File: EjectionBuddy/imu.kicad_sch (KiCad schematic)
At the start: 5 parts, among them U8 MPU-6050

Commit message: Side-mcu stm -> attiny, with improvements here and there
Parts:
- renumbered C18 to C17, C19 to C18, C20 to C19, C21 to C20
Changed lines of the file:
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@@
 		(on_board yes)
 		(dnp no)
-		(property "Reference" "#PWR0120"
+		(property "Reference" "#PWR0121"
 			(at 54.61 38.1 0)
 			(effects
@@
 			(project "EjectionBuddy"
 				(path "/8eb0a75f-d01a-4f77-b089-39fac6868a70/fc114c64-d761-4020-b59c-5aa26268bf21"
-					(reference "#PWR0120")
+					(reference "#PWR0121")
 					(unit 1)
 				)
@@
 		(on_board yes)
 		(dnp no)
-		(property "Reference" "C19"
+		(property "Reference" "C18"
 			(at 81.28 41.9099 0)
 			(effects
@@
 			(project "EjectionBuddy"
 				(path "/8eb0a75f-d01a-4f77-b089-39fac6868a70/fc114c64-d761-4020-b59c-5aa26268bf21"
-					(reference "C19")
+					(reference "C18")
 					(unit 1)
 				)
@@
 		(dnp no)
 		(fields_autoplaced yes)
-		(property "Reference" "#PWR0122"
+		(property "Reference" "#PWR0123"
 			(at 54.61 55.88 0)
 			(effects
@@
 			(project "EjectionBuddy"
 				(path "/8eb0a75f-d01a-4f77-b089-39fac6868a70/fc114c64-d761-4020-b59c-5aa26268bf21"
-					(reference "#PWR0122")
+					(reference "#PWR0123")
 					(unit 1)
 				)
@@
 		(dnp no)
 		(fields_autoplaced yes)
-		(property "Reference" "#PWR0125"
+		(property "Reference" "#PWR0126"
 			(at 45.72 99.06 0)
 			(effects
@@
 			(project "EjectionBuddy"
 				(path "/8eb0a75f-d01a-4f77-b089-39fac6868a70/fc114c64-d761-4020-b59c-5aa26268bf21"
-					(reference "#PWR0125")
+					(reference "#PWR0126")
 					(unit 1)
 				)
@@
 		(on_board yes)
 		(dnp no)
-		(property "Reference" "#PWR0124"
+		(property "Reference" "#PWR0125"
 			(at 92.71 68.58 0)
 			(effects
@@
 			(project "EjectionBuddy"
 				(path "/8eb0a75f-d01a-4f77-b089-39fac6868a70/fc114c64-d761-4020-b59c-5aa26268bf21"
-					(reference "#PWR0124")
+					(reference "#PWR0125")
 					(unit 1)
 				)
@@
 		(dnp no)
 		(fields_autoplaced yes)
-		(property "Reference" "#PWR0127"
+		(property "Reference" "#PWR0128"
 			(at 92.71 99.06 0)
 			(effects
@@
 			(project "EjectionBuddy"
 				(path "/8eb0a75f-d01a-4f77-b089-39fac6868a70/fc114c64-d761-4020-b59c-5aa26268bf21"
-					(reference "#PWR0127")
+					(reference "#PWR0128")
 					(unit 1)
 				)
@@
 		(on_board yes)
 		(dnp no)
-		(property "Reference" "C20"
+		(property "Reference" "C19"
 			(at 96.52 69.8499 0)
 			(effects
@@
 			(project "EjectionBuddy"
 				(path "/8eb0a75f-d01a-4f77-b089-39fac6868a70/fc114c64-d761-4020-b59c-5aa26268bf21"
-					(reference "C20")
+					(reference "C19")
 					(unit 1)
 				)
@@
 		(on_board yes)
 		(dnp no)
-		(property "Reference" "C18"
+		(property "Reference" "C17"
 			(at 58.42 41.9099 0)
 			(effects
@@
 			(project "EjectionBuddy"
 				(path "/8eb0a75f-d01a-4f77-b089-39fac6868a70/fc114c64-d761-4020-b59c-5aa26268bf21"
-					(reference "C18")
+					(reference "C17")
 					(unit 1)
 				)
@@
 		(on_board yes)
 		(dnp no)
-		(property "Reference" "C21"
+		(property "Reference" "C20"
 			(at 96.52 85.0899 0)
 			(effects
@@
 			(project "EjectionBuddy"
 				(path "/8eb0a75f-d01a-4f77-b089-39fac6868a70/fc114c64-d761-4020-b59c-5aa26268bf21"
-					(reference "C21")
+					(reference "C20")
 					(unit 1)
 				)
@@
 		(on_board yes)
 		(dnp no)
-		(property "Reference" "#PWR0121"
+		(property "Reference" "#PWR0122"
 			(at 77.47 38.1 0)
 			(effects
@@
 			(project "EjectionBuddy"
 				(path "/8eb0a75f-d01a-4f77-b089-39fac6868a70/fc114c64-d761-4020-b59c-5aa26268bf21"
-					(reference "#PWR0121")
+					(reference "#PWR0122")
 					(unit 1)
 				)
@@
 		(dnp no)
 		(fields_autoplaced yes)
-		(property "Reference" "#PWR0123"
+		(property "Reference" "#PWR0124"
 			(at 77.47 55.88 0)
 			(effects
@@
 			(project "EjectionBuddy"
 				(path "/8eb0a75f-d01a-4f77-b089-39fac6868a70/fc114c64-d761-4020-b59c-5aa26268bf21"
-					(reference "#PWR0123")
+					(reference "#PWR0124")
 					(unit 1)
 				)
@@
 		(dnp no)
 		(fields_autoplaced yes)
-		(property "Reference" "#PWR0126"
+		(property "Reference" "#PWR0127"
 			(at 66.04 99.06 0)
 			(effects
@@
 			(project "EjectionBuddy"
 				(path "/8eb0a75f-d01a-4f77-b089-39fac6868a70/fc114c64-d761-4020-b59c-5aa26268bf21"
-					(reference "#PWR0126")
-					(unit 1)
-				)
+					(reference "#PWR0127")
+					(unit 1)
+				)

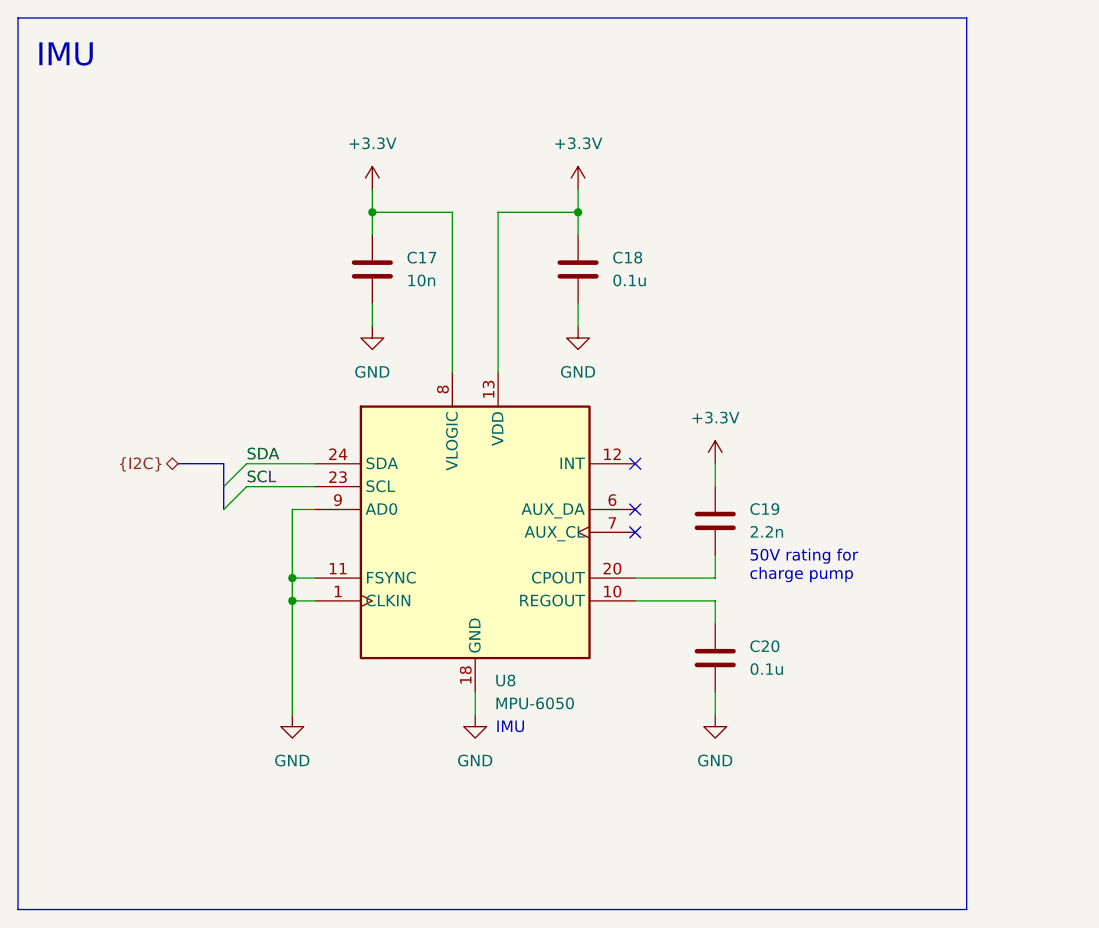
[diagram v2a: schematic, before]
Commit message: Fixed a FATAL imu wiring fault, CPOUT
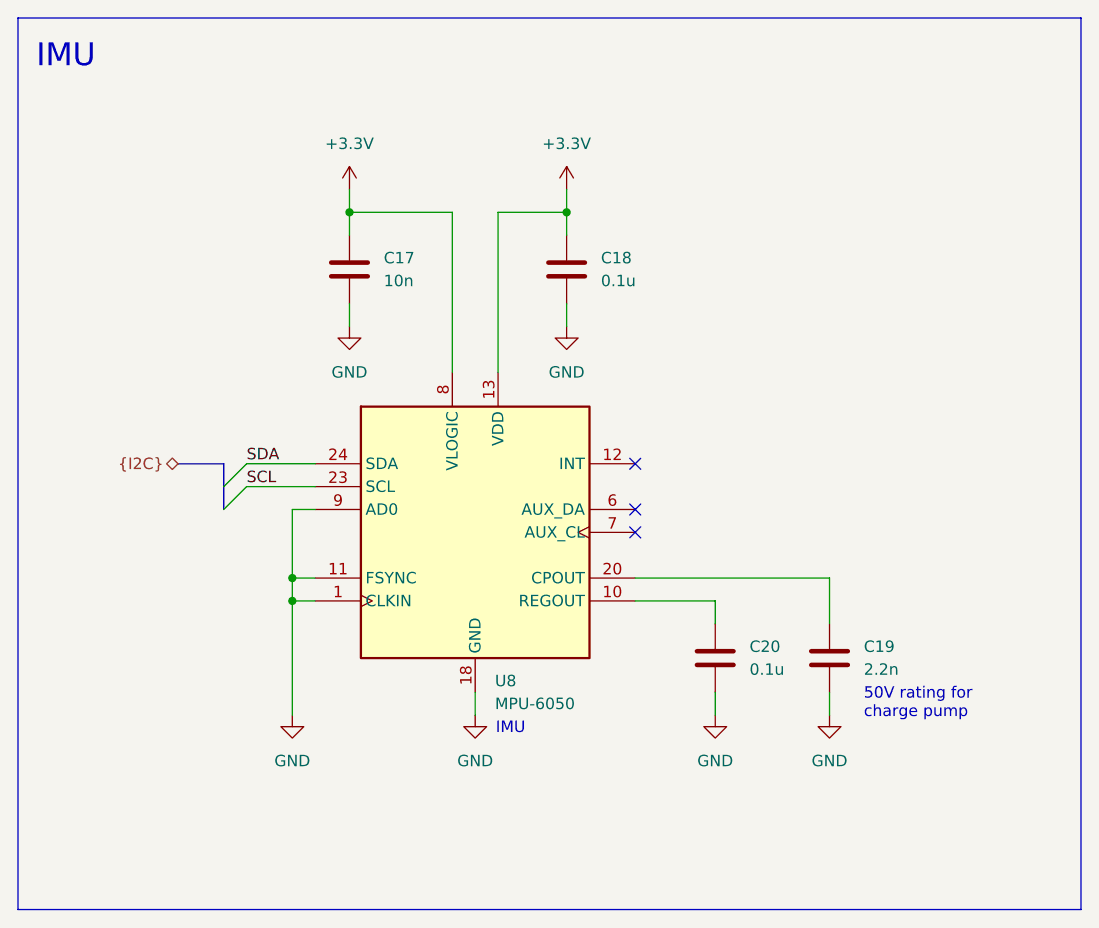
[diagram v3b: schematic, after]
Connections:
- net +3.3V: no longer C19.1
- net GND: now also C19.2
- net at U8.20 (CPOUT): now also C19.1; no longer C19.2
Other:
- moved on the sheet: C17, C18, C19
